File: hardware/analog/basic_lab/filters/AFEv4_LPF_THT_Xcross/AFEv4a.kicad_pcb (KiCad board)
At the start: 2 copper layers, 40.1 x 53.8 mm, 14 parts, among them J3 Connector_Generic_Conn_01x02, J4 Connector_Generic_Conn_01x02, J5 Connector_Generic_Conn_01x02, J6 Connector_Generic_Conn_01x02, J7 Connector_Generic_Conn_01x02, J8 Connector_Generic_Conn_01x02, J9 Connector_Generic_Conn_01x02

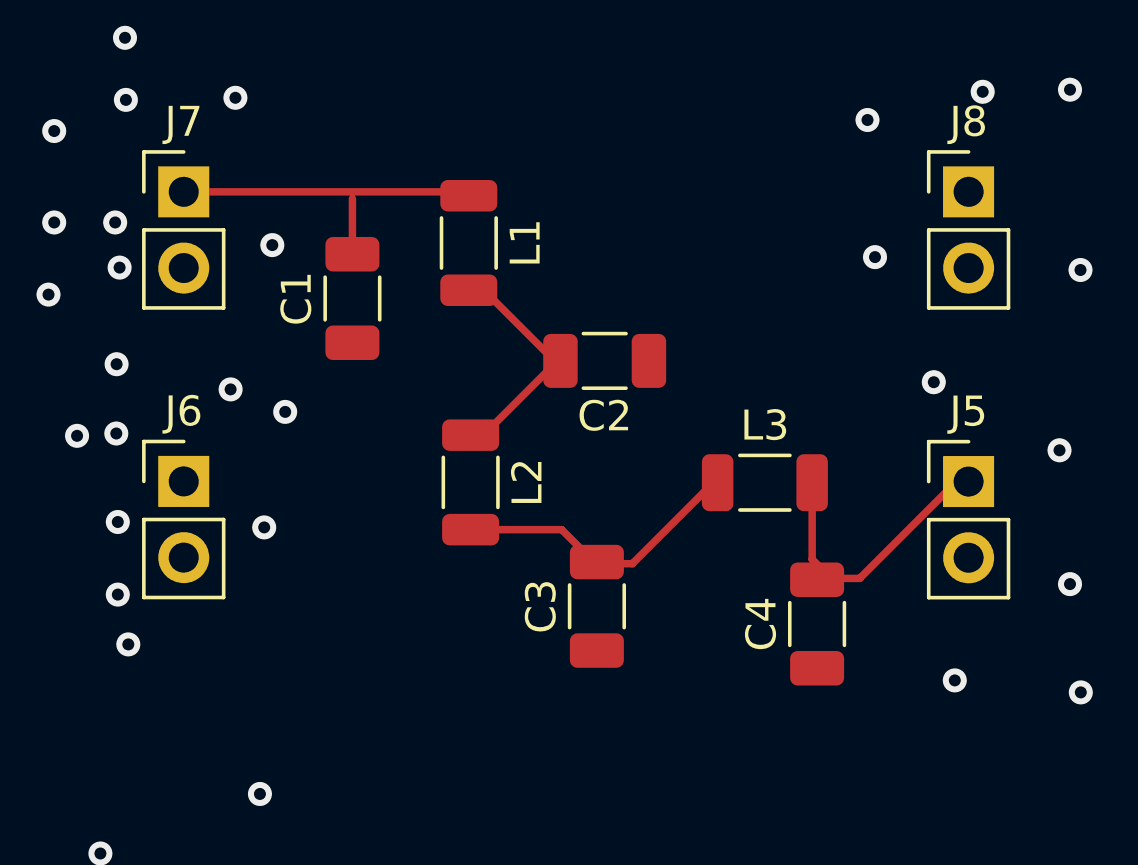
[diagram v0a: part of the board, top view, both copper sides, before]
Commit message: started PCB THT LPF
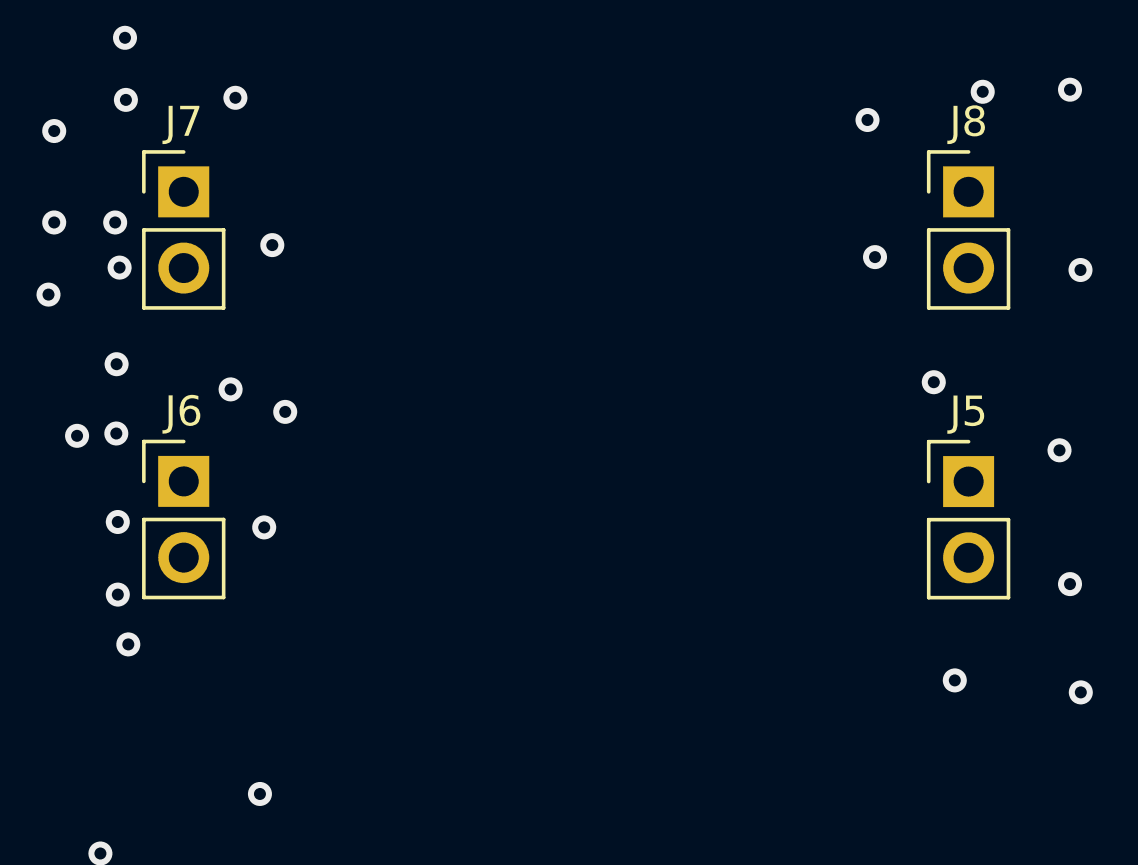
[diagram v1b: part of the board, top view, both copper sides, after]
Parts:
- removed C1, C2, C3, C4: C, Capacitor_SMD:C_1206_3216Metric
- removed L1, L2, L3: L, Inductor_SMD:L_1206_3216Metric
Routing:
- net bpf_lvds: track 11.7 -> 0.00 mm
- net Net-(C3-Pad2): track 9.64 -> 0.00 mm
- net bpf_ant: track 8.87 -> 0.00 mm
- net Net-(C2-Pad2): track 7.50 -> 0.00 mm

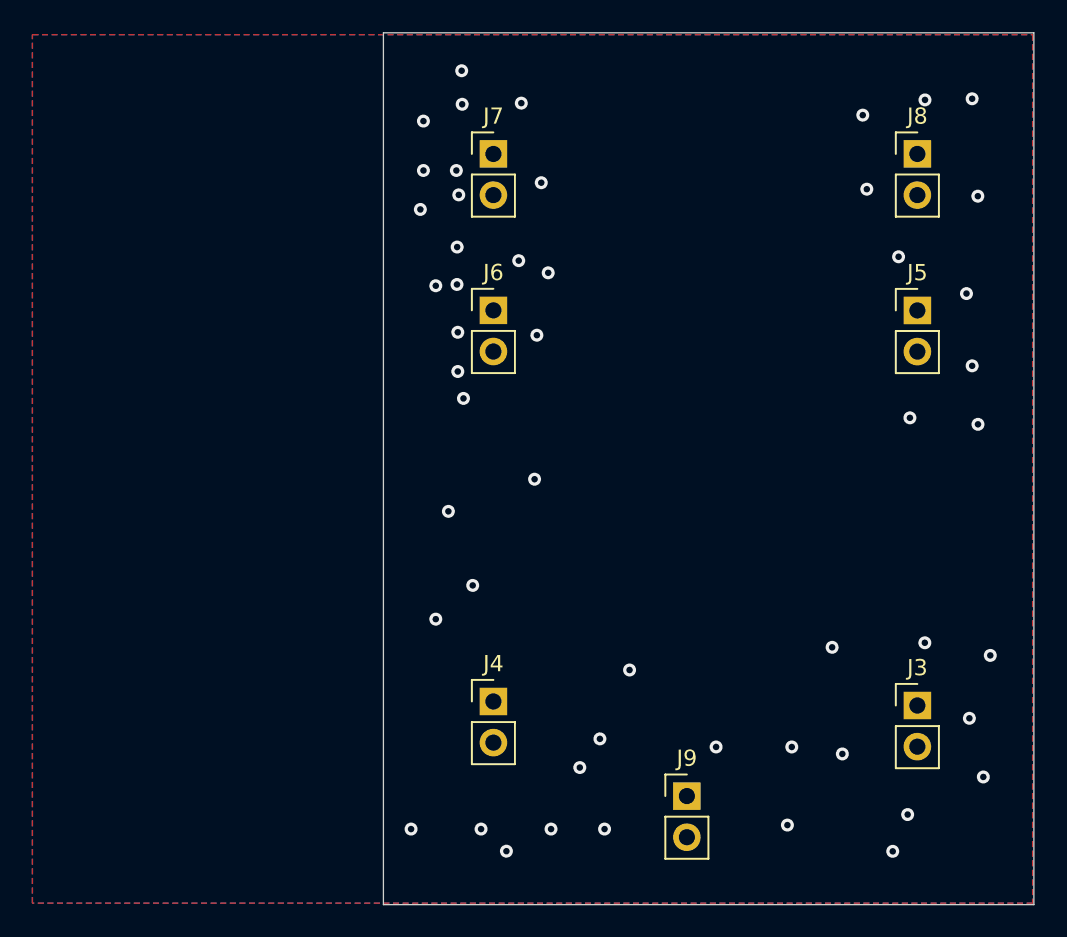
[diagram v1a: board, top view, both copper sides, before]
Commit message: started PCB THT LPF
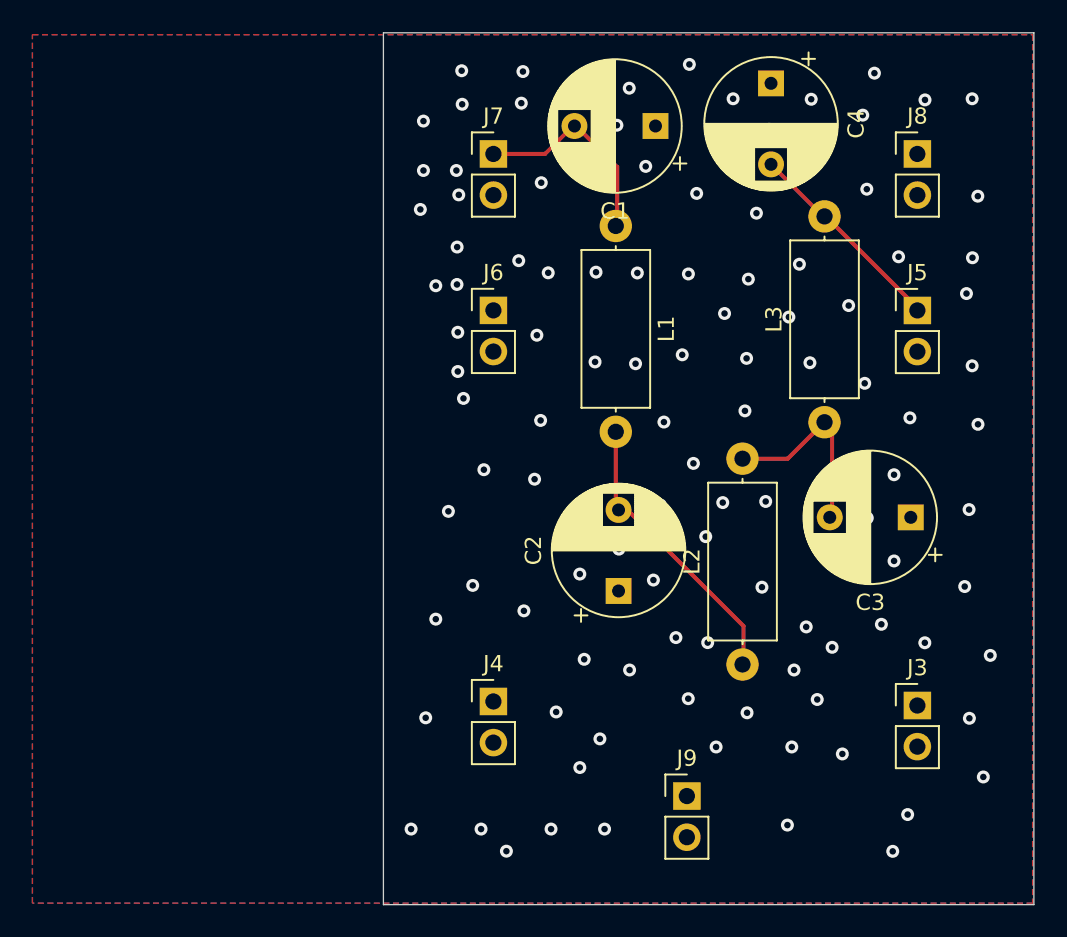
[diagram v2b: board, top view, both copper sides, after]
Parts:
- added C1: 270pF, Capacitor_THT:CP_Radial_D8.0mm_P5.00mm, F.Cu at (89.2, 79.5)
- added C2: 680pF, Capacitor_THT:CP_Radial_D8.0mm_P5.00mm, F.Cu at (87.0, 108.2)
- added C3: 270pF, Capacitor_THT:CP_Radial_D8.0mm_P5.00mm, F.Cu at (105.0, 103.7)
- added C4: 680pF, Capacitor_THT:CP_Radial_D8.0mm_P5.00mm, F.Cu at (96.4, 76.9)
- added L1: 1.5uH, Inductor_THT:L_Axial_L9.5mm_D4.0mm_P12.70mm_Horizontal_Fastron_SMCC, F.Cu at (86.8, 85.7)
- added L2: 1.8uH, Inductor_THT:L_Axial_L9.5mm_D4.0mm_P12.70mm_Horizontal_Fastron_SMCC, F.Cu at (94.6, 112.8)
- added L3: 1.5uH, Inductor_THT:L_Axial_L9.5mm_D4.0mm_P12.70mm_Horizontal_Fastron_SMCC, F.Cu at (99.7, 97.8)
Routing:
- net Net-(C2-Pad2): track 0.00 -> 17.9 mm
- net bpf_lvds: track 0.00 -> 13.2 mm
- net bpf_ant: track 0.00 -> 13.0 mm
- net Net-(C3-Pad2): track 0.00 -> 12.0 mm
- net GND: vias 51 -> 114
